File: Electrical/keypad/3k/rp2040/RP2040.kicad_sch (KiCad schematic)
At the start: 85 parts, among them J1 Conn_01x04_Socket, J2 Conn_01x04_Socket, P1 USB-TYPE-C-016, Q1 BSS138, Q2 BSS138, SW1 KAN0644-0551B1-A, SW2 KAN0644-0551B1-A, SW3 KAN0644-0551B1-A, SW4 TS-1187A-B-A-B, SW5 TS-1187A-B-A-B, U1 ME6212C33M5G, U2 W25Q16JVSS, U3 PRTR5V0U2X, U4 RP2040, U5 SLSS49E, U6 SLSS49E, U7 SLSS49E, Y1 12MHz

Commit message: puts in more led
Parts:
- removed D4: WS2812B, LED_SMD:LED_WS2812B_PLCC4_5.0x5.0mm_P3.2mm, symbol LED:WS2812B
- removed J1: Conn_01x04_Socket, Connector_PinSocket_2.54mm:PinSocket_1x04_P2.54mm_Vertical, symbol Connector:Conn_01x04_Socket
- added C35: 100n, Capacitor_SMD:C_0402_1005Metric, symbol Device:C
- added D11, D4: WS2812-2020, footprints:LED_WS2812-2020, symbol WS2812-2020:WS2812-2020
- added J1: Conn_01x02_Socket, Connector_PinSocket_2.54mm:PinSocket_1x02_P2.54mm_Vertical, symbol Connector:Conn_01x02_Socket
- renumbered C35 to C36, C36 to C37, C37 to C38, D11 to D12, D12 to D13, D13 to D14, D14 to D15
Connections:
- net +5V: now also C35.1, D11.1 (VDD), D4.1 (VDD)
- net GND: now also C35.2, D11.3 (GND), D4.3 (GND)
- net SCL_1: now also J1.2 (Pin_2)
- net SDA_1: now also J1.1 (Pin_1)
- net at D5.4 (DIN): now also D4.2 (DO)
- net at D3.2 (DO): now also D4.4 (DI)
- net at D10.2 (DO): now also D11.4 (DI); no longer D12.4 (DIN)
- net SCL_0 renamed GPIO21
- net SDA_0 renamed GPIO20
- new net: D11.2 (DO), D12.4 (DIN)
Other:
- moved on the sheet: C34, D12

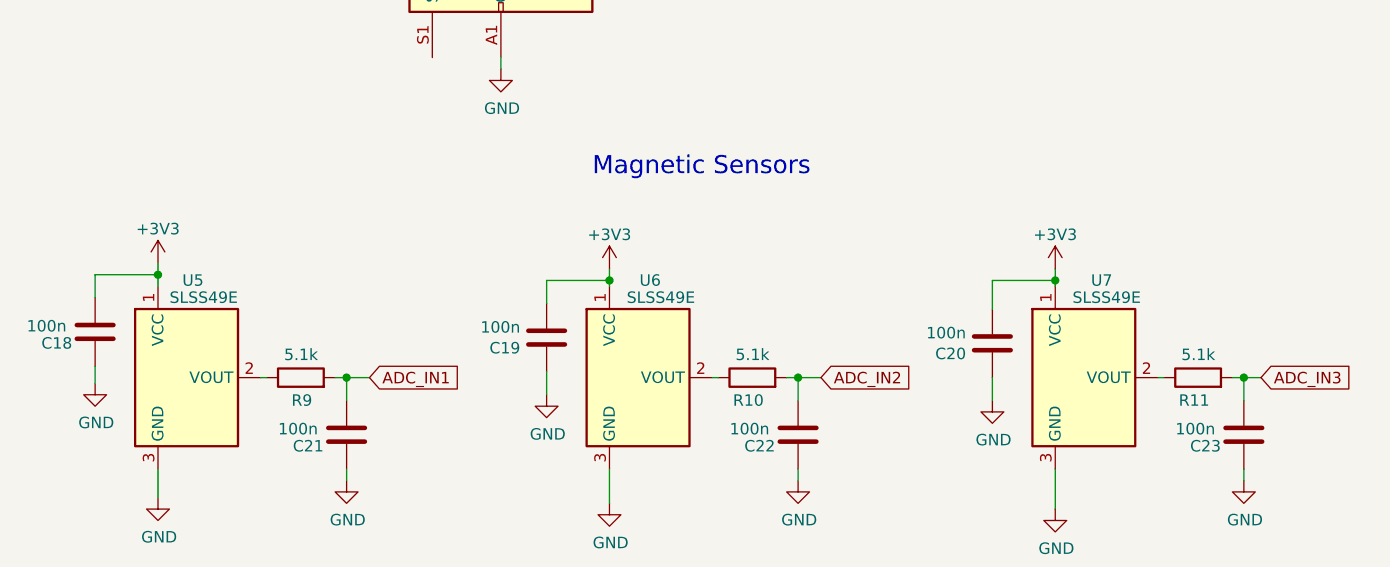
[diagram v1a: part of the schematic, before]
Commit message: changes slss49 to DRV
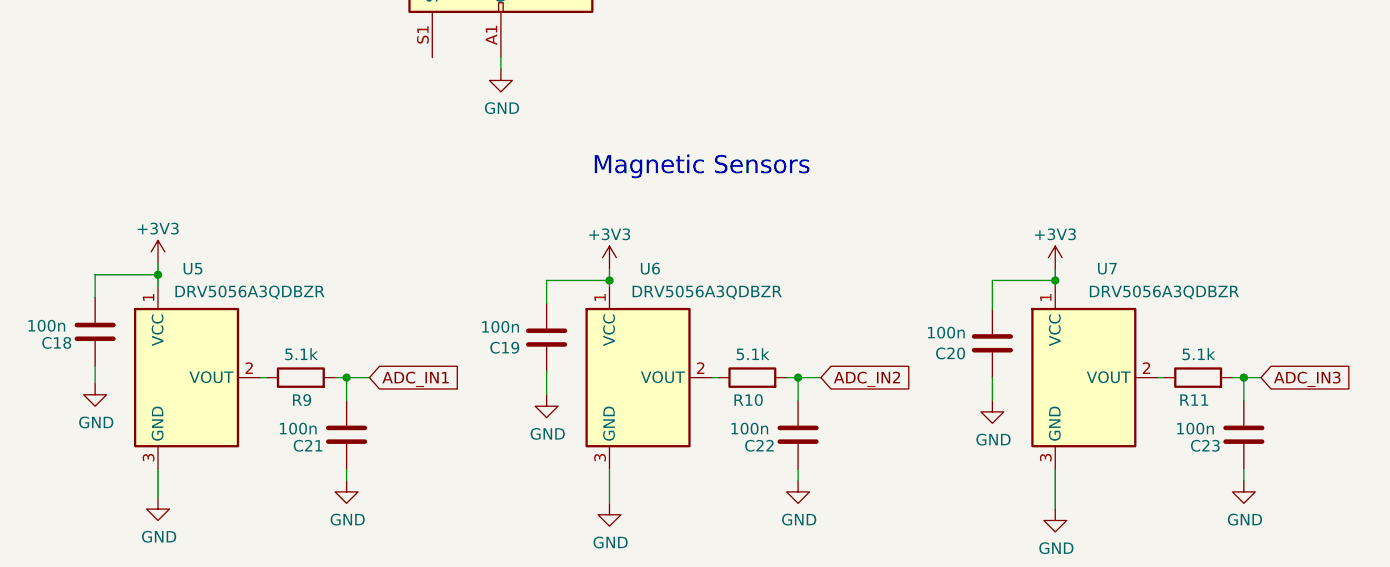
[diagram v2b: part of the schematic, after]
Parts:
- U5, U6, U7: value SLSS49E -> DRV5056A3QDBZR
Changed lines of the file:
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@@
   (symbol (lib_id "Sensor_Magnetic:SLSS49E") (at 371.475 159.385 0) (unit 1)
     (in_bom yes) (on_board yes) (dnp no)
-    (property "Reference" "U7" (at 374.015 148.59 0)
+    (property "Reference" "U7" (at 374.65 147.32 0)
       (effects (font (size 1.27 1.27)) (justify right))
     )
-    (property "Value" "SLSS49E" (at 373.38 150.495 0)
+    (property "Value" "DRV5056A3QDBZR" (at 379.73 149.86 0)
       (effects (font (size 1.27 1.27)))
     )
@@
   (symbol (lib_id "Sensor_Magnetic:SLSS49E") (at 321.945 159.385 0) (unit 1)
     (in_bom yes) (on_board yes) (dnp no)
-    (property "Reference" "U6" (at 323.85 148.59 0)
+    (property "Reference" "U6" (at 323.85 147.32 0)
       (effects (font (size 1.27 1.27)) (justify right))
     )
-    (property "Value" "SLSS49E" (at 323.85 150.495 0)
+    (property "Value" "DRV5056A3QDBZR" (at 328.93 149.86 0)
       (effects (font (size 1.27 1.27)))
     )
@@
   (symbol (lib_id "Sensor_Magnetic:SLSS49E") (at 271.78 159.385 0) (unit 1)
     (in_bom yes) (on_board yes) (dnp no)
-    (property "Reference" "U5" (at 273.05 148.59 0)
+    (property "Reference" "U5" (at 273.05 147.32 0)
       (effects (font (size 1.27 1.27)) (justify right))
     )
-    (property "Value" "SLSS49E" (at 273.05 150.495 0)
-      (effects (font (size 1.27 1.27)))
-    )
+    (property "Value" "DRV5056A3QDBZR" (at 278.13 149.86 0)
+      (effects (font (size 1.27 1.27)))
+    )

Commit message: finishes pcb
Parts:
- R1: footprint Capacitor_SMD:C_0402_1005Metric -> Resistor_SMD:R_0402_1005Metric
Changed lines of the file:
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@@
       (effects (font (size 1.27 1.27)) (justify left))
     )
-    (property "Footprint" "Capacitor_SMD:C_0402_1005Metric" (at 50.927 50.165 90)
+    (property "Footprint" "Resistor_SMD:R_0402_1005Metric" (at 50.927 50.165 90)
       (effects (font (size 1.27 1.27)) hide)
     )

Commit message: switches back to 1 data pin for LED
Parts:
- removed Q2: BSS138, Package_TO_SOT_SMD:SOT-23, symbol Transistor_FET:BSS138
- removed R14, R15: 10k, Resistor_SMD:R_0402_1005Metric, symbol Device:R_Small
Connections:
- net at D13.4 (DI): now also D12.2 (DOUT)
- net BL_LED_D renamed LED_D
- net LED_D: now also Q1.2 (S), R12.1
- removed net U_LED_D: Q1.2 (S), R12.1, U4.16 (GPIO13)
- new net GPIO13: U4.16 (GPIO13)
